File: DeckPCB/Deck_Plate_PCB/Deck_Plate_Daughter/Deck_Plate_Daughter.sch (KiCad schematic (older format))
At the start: 32 parts, among them J1 SunnyBuddy_Inhibit, J2 JST_Batt_Conn, J3 Motor_Inhibit, J4 BurnWire_Inhibit, J5 Power, J6 Raspberry_Pi_2_3, J7 Board_to_Board, J8 SensorEndPanel, J9 Payload_NextFlex, U2 SunnyBuddy_Breakout, U3 Big_Easy_Driver, U5 Adafruit_INA219_Breakout

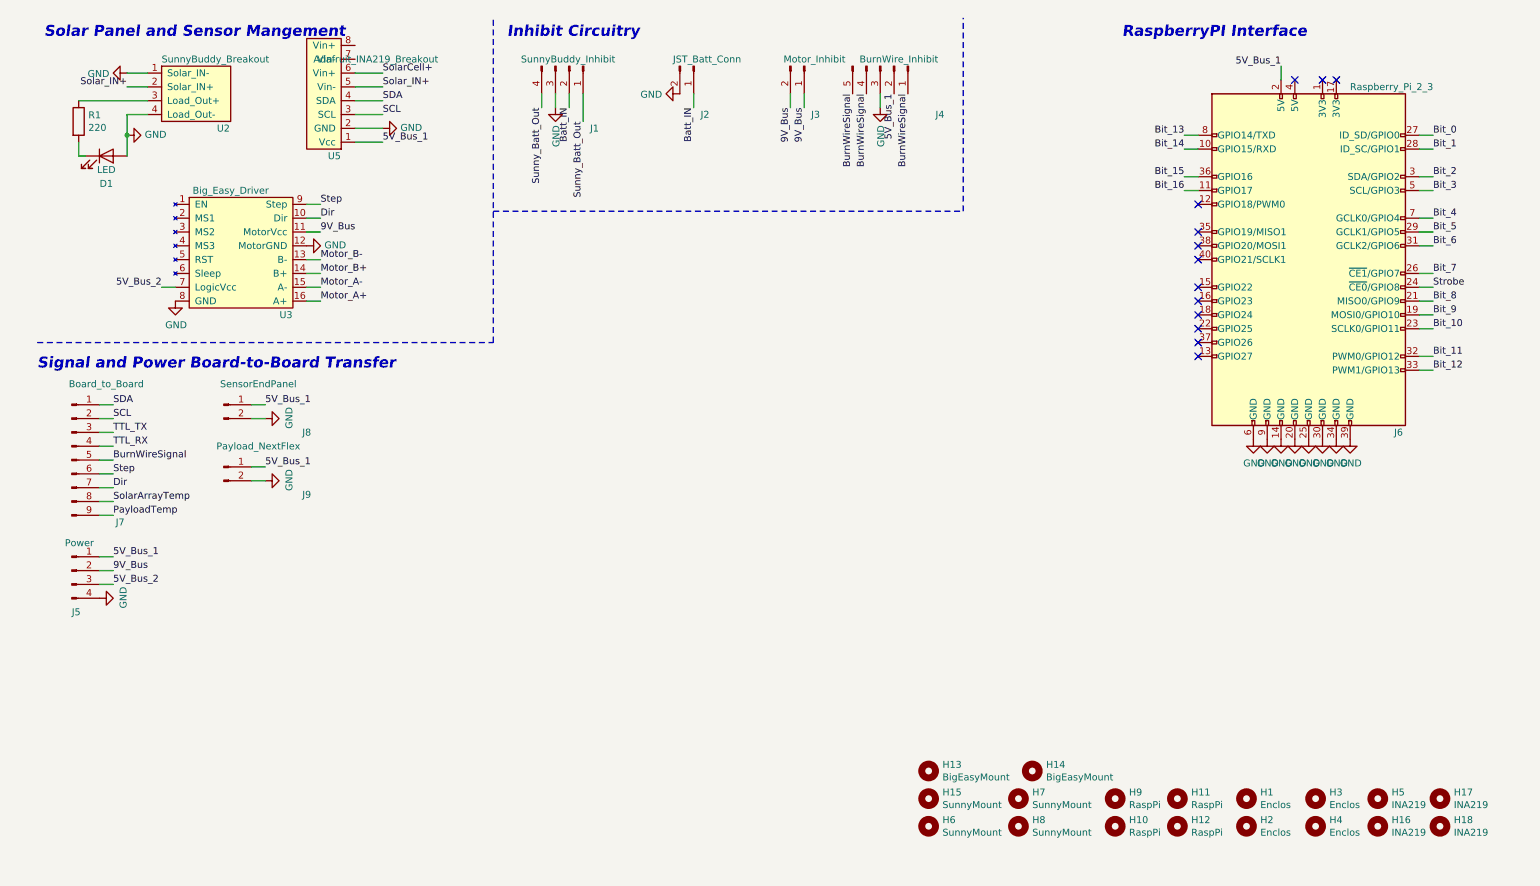
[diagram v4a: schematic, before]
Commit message: Updated Main_Deck_Plate and Daughter_Board to fit Electronics Enclosure internal dimensions. Created all PCB Gerber files. Created all PCB PNG images. Created all PCB STEP files for mechanical integration. Implemented all design review comments and corrections.
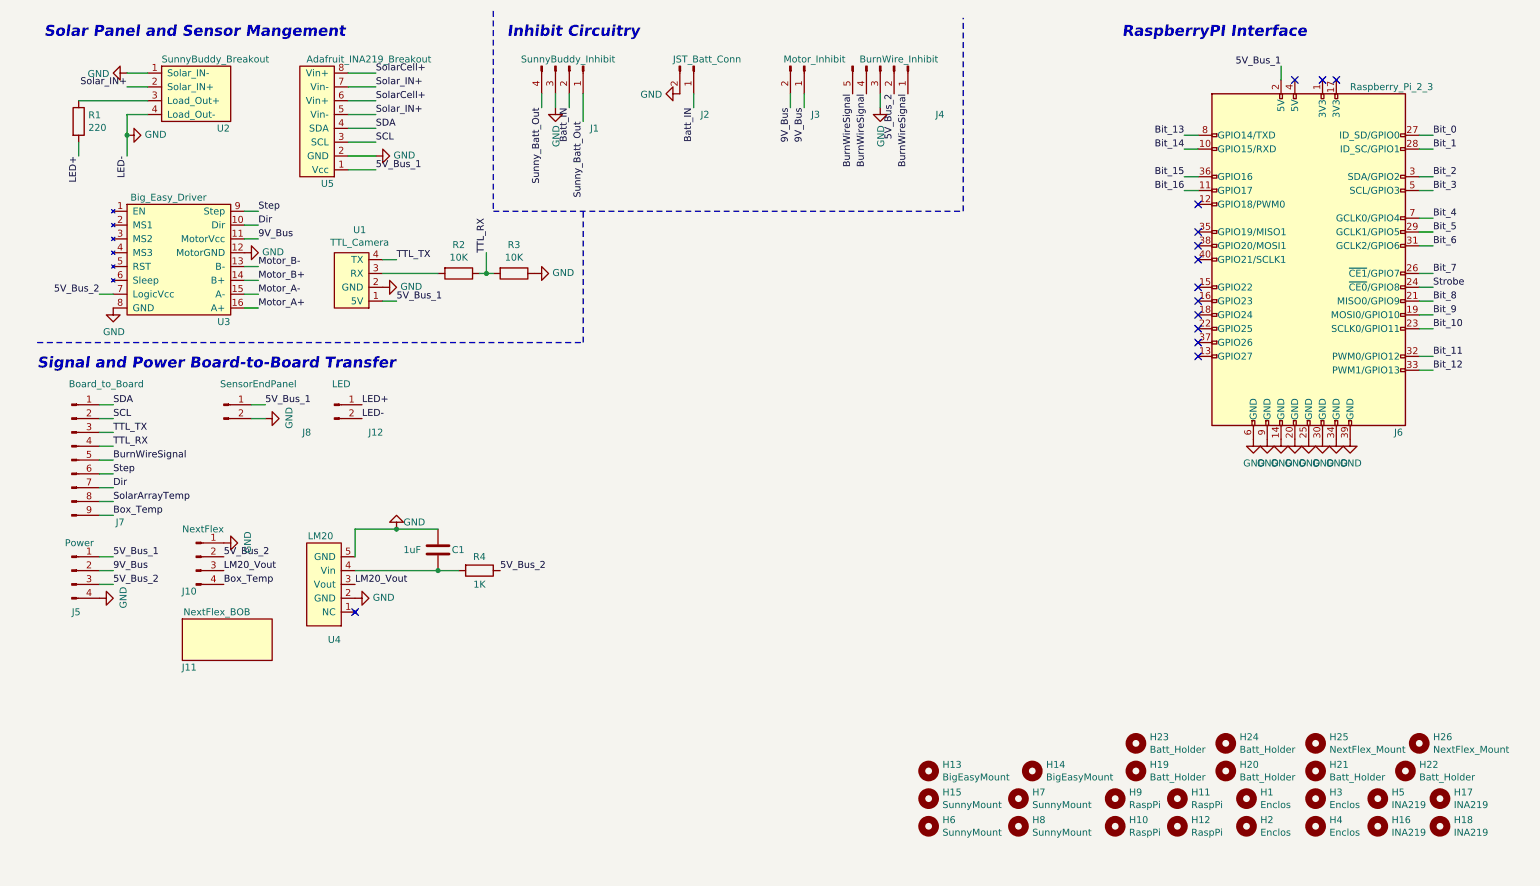
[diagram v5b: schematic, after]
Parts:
- removed D1: LED, LED_THT:LED_D3.0mm, symbol Device:LED
- removed J9: Payload_NextFlex, Connector_PinHeader_2.54mm:PinHeader_1x02_P2.54mm_Vertical, symbol Connector:Conn_01x02_Male
- added C1: 1uF, Capacitor_THT:C_Axial_L3.8mm_D2.6mm_P7.50mm_Horizontal, symbol Device:C
- added H19, H20, H21, H22, H23, H24: Batt_Holder, MountingHole:MountingHole_5.3mm_M5, symbol Mechanical:MountingHole
- added H25, H26: NextFlex_Mount, Deck_Plate_PCB:NextFlex_Mount_3mm, symbol Mechanical:MountingHole
- added J10: NextFlex, Connector_PinHeader_2.54mm:PinHeader_1x04_P2.54mm_Vertical, symbol Connector:Conn_01x04_Male
- added J11: NextFlex_BOB, Deck_Plate_PCB:NextFlex, symbol Deck_Plate_PCB:NextFlex_BOB
- added J12: LED, Connector_PinHeader_2.54mm:PinHeader_1x02_P2.54mm_Vertical, symbol Connector:Conn_01x02_Male
- added R2, R3: 10K, Resistor_THT:R_Axial_DIN0207_L6.3mm_D2.5mm_P10.16mm_Horizontal, symbol Device:R
- added R4: 1K, Resistor_THT:R_Axial_DIN0207_L6.3mm_D2.5mm_P10.16mm_Horizontal, symbol Device:R
- added U1: TTL_Camera, Connector_PinHeader_2.54mm:PinHeader_1x04_P2.54mm_Vertical, symbol Deck_Plate_PCB:TTL_Camera
- added U4: LM20, Package_TO_SOT_SMD:SOT-353_SC-70-5_Handsoldering, symbol Deck_Plate_PCB:LM20
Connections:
- net 5V_Bus_1: now also U1.1 (5V); no longer J4.2 (Pin_2)
- net 5V_Bus_2: now also J4.2 (Pin_2), J10.2 (Pin_2), R4.1
- net GND: now also C1.2, J10.1 (Pin_1), J12.2 (Pin_2), R3.1, U1.2 (GND), U4.2 (GND), U4.5 (GND)
- net SolarCell+: now also U5.8 (Vin+)
- net Solar_IN+: now also U5.7 (Vin-)
- net TTL_RX: now also R2.1, R3.2
- net TTL_TX: now also U1.4 (TX)
- net LED+: now reaches R1.2
- net LED+: now also J12.1 (Pin_1)
- net PayloadTemp renamed Box_Temp
- net Box_Temp: now also J10.4 (Pin_4)
- new net: R2.2, U1.3 (RX)
- new net: C1.1, R4.2, U4.4 (Vin)
- new net LM20_Vout: J10.3 (Pin_3), U4.3 (Vout)
- no-connect marks 13 -> 14
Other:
- moved on the sheet: U3, U5
